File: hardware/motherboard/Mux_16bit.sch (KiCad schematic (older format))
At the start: 13 parts, among them U1 SN74ALVC00, U10 SN74ALVC00, U11 SN74ALVC00, U12 SN74ALVC00, U13 SN74ALVC00, U2 SN74ALVC00, U3 SN74ALVC00, U4 SN74ALVC00, U5 SN74ALVC00, U6 SN74ALVC00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

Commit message: All boards as fabbed at v1.0
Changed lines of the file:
@@
 NoConn ~ 9000 5450
 NoConn ~ 9000 5900
+Text HLabel 1650 1400 2    50   Output ~ 0
+not_sel
 $EndSCHEMATC

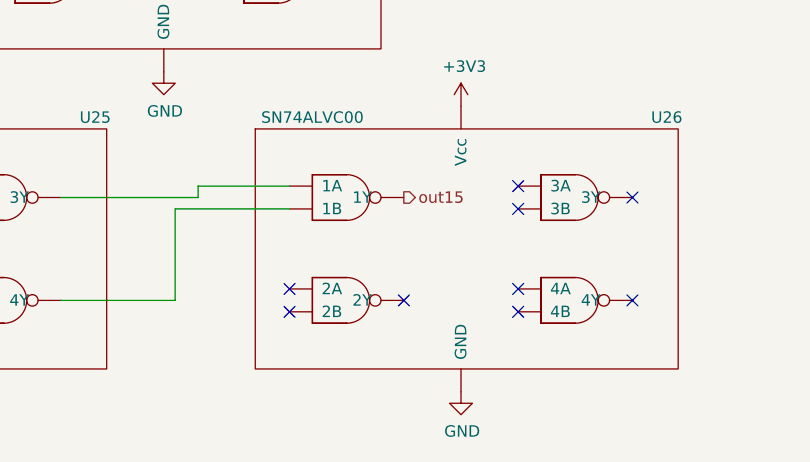
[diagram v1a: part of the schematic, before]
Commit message: Motherboard: Added power switch, moved reset switch, modified silkscreens for readability, fixed A-register connector pinout, grounded NC input pins, changed paste layer clearance to -0.05mm
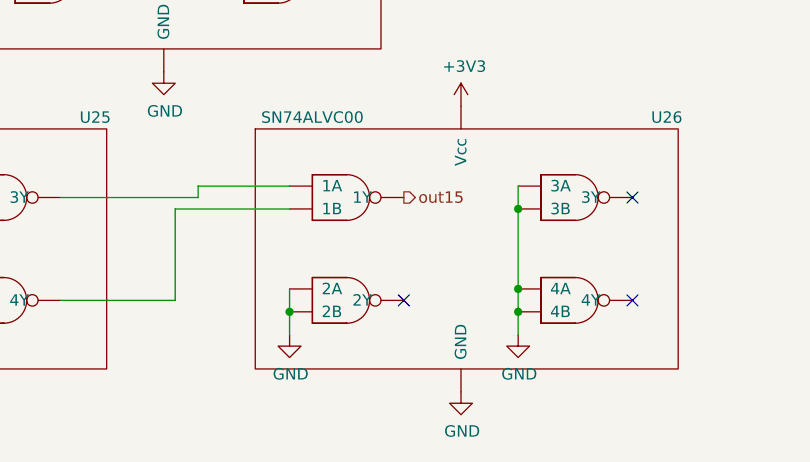
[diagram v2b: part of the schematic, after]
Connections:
- net GND: now also U13.10 (3B), U13.12 (4A), U13.13 (4B), U13.4 (2A), U13.5 (2B), U13.9 (3A)
- no-connect marks 9 -> 3
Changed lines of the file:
@@
 	1    0    0    -1
 $EndComp
-NoConn ~ 7500 5850
-NoConn ~ 7500 5950
 NoConn ~ 8000 5900
-NoConn ~ 8500 5400
-NoConn ~ 8500 5500
-NoConn ~ 8500 5850
-NoConn ~ 8500 5950
 NoConn ~ 9000 5450
 NoConn ~ 9000 5900
 Text HLabel 1650 1400 2    50   Output ~ 0
 not_sel
+Wire Wire Line
+	8500 5400 8500 5500
+Connection ~ 8500 5500
+Wire Wire Line
+	8500 5500 8500 5850
+Connection ~ 8500 5850
+Wire Wire Line
+	8500 5850 8500 5950
+Connection ~ 8500 5950
+Wire Wire Line
+	8500 5950 8500 6050
+Wire Wire Line
+	7500 5850 7500 5950
+Connection ~ 7500 5950
+Wire Wire Line
+	7500 5950 7500 6050
+$Comp
+L power:GND #PWR051
+U 1 1 5EE7F347
+P 7500 6050
+AR Path="/5E81995D/5EE7F347" Ref="#PWR051"  Part="1"
+AR Path="/5EAF9122/5EE7F347" Ref="#PWR065"  Part="1"
+F 0 "#PWR065" H 7500 5800 50  0001 C CNN
+F 1 "GND" H 7505 5877 50  0000 C CNN
+F 2 "" H 7500 6050 50  0001 C CNN
+F 3 "" H 7500 6050 50  0001 C CNN
+	1    7500 6050
+	1    0    0    -1
+$EndComp
+$Comp
+L power:GND #PWR064
+U 1 1 5EE7F760
+P 8500 6050
+AR Path="/5E81995D/5EE7F760" Ref="#PWR064"  Part="1"
+AR Path="/5EAF9122/5EE7F760" Ref="#PWR066"  Part="1"
+F 0 "#PWR066" H 8500 5800 50  0001 C CNN
+F 1 "GND" H 8505 5877 50  0000 C CNN
+F 2 "" H 8500 6050 50  0001 C CNN
+F 3 "" H 8500 6050 50  0001 C CNN
+	1    8500 6050
+	1    0    0    -1
+$EndComp
 $EndSCHEMATC
